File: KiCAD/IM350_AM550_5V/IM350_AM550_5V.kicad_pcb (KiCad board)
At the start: 2 copper layers, 12 parts, among them J5 USB_B_Micro_Power, J7 RJ12, P3 0R, P4 0R, SW1 Pairing, U1 MCP1700-3302E_SOT23, U2 ESP-12F

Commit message: Update
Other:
- board outline added: 59 x 20 mm

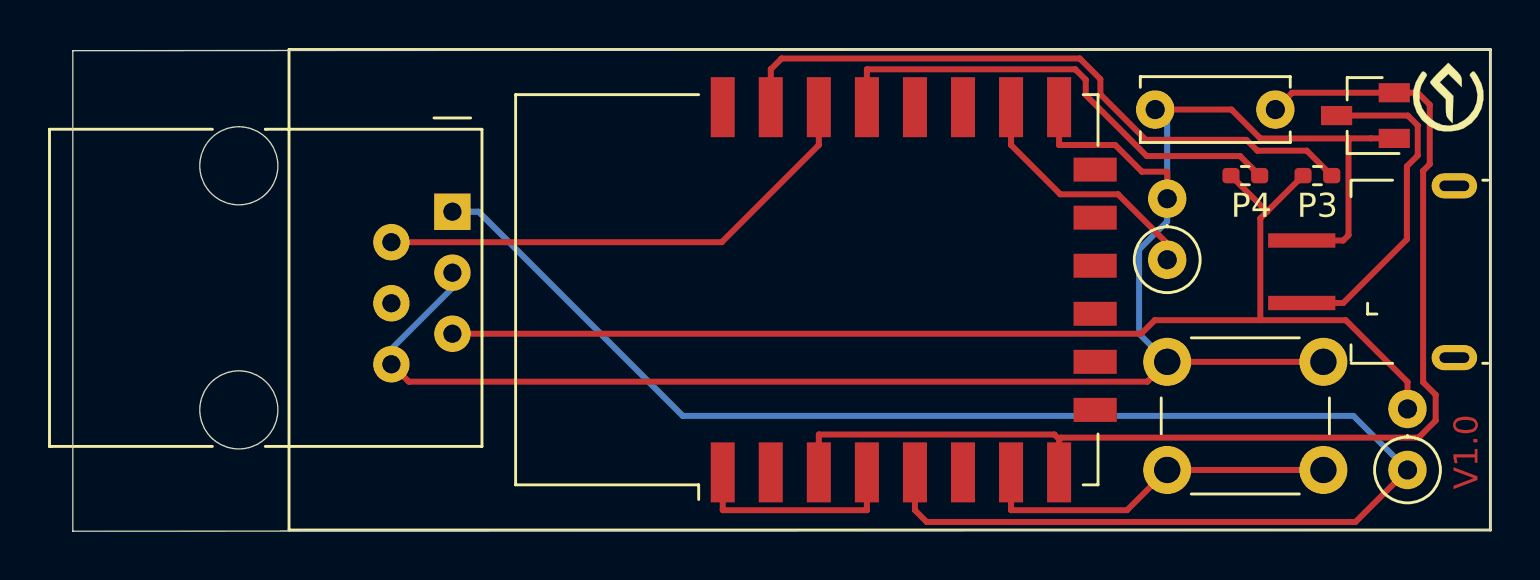
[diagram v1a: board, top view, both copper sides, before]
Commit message: Website handleSettings bugfix
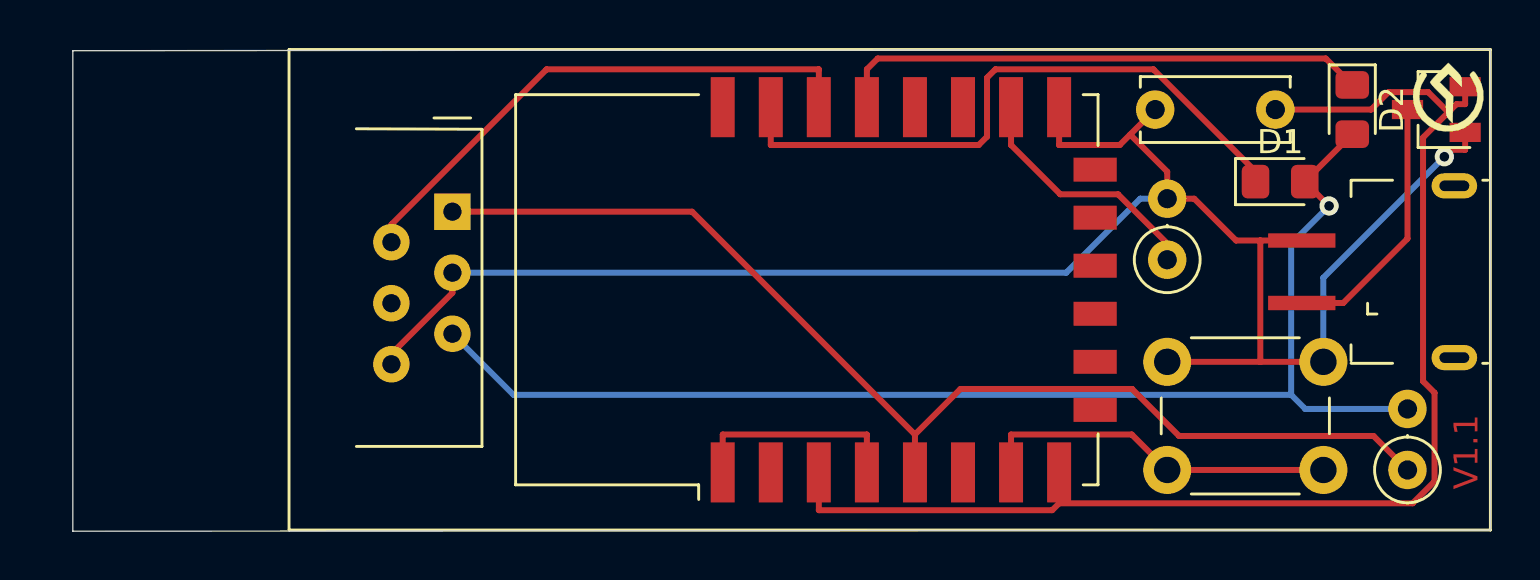
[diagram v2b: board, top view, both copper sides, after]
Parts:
- removed P3, P4: 0R, Resistor_SMD:R_0402_1005Metric_Pad0.72x0.64mm_HandSolder
- added D1: 1N4148, Diode_SMD:D_0805_2012Metric_Pad1.15x1.40mm_HandSolder, F.Cu at (82.0, 39.5)
- added D2: 1N4148, Diode_SMD:D_0805_2012Metric_Pad1.15x1.40mm_HandSolder, F.Cu at (85.0, 36.5)
- J7: footprint Connector_RJ:RJ12_Amphenol_54601 -> ErichCollection:RJ12_Amphenol_54601_Reduced
- moved U1 2.96 mm to (88.5, 36.5)
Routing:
- net Net-(J7-Pad1): track 67.4 -> 47.3 mm
- net +3V3: track 49.4 -> 54.4 mm
- net Net-(C2-Pad2): track 80.1 -> 75.6 mm, vias 0 -> 1
- net Net-(J5-Pad1): track 13.9 -> 10.9 mm
- net Net-(D1-Pad2): track 51.0 -> 53.8 mm, vias 0 -> 1
- net /GPIO4: track 20.1 -> 22.4 mm
- net Net-(J7-Pad2): track 21.0 -> 22.8 mm
- net /GPIO3: track 27.5 -> 26.7 mm
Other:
- board text added: "V1.1"
- board text removed: "V1.0"
